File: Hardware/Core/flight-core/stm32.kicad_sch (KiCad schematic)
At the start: 32 parts, among them J7 Conn_01x04_Socket, SW1 SW_Push, SW2 SW_Push, U1 TCAN1042VDRQ1, U2 STM32G473CCTx, U3 MCP23S17_SS, U4 MAX7221xWG, U5 CC56-12SEKWA, Y1 48 MHz

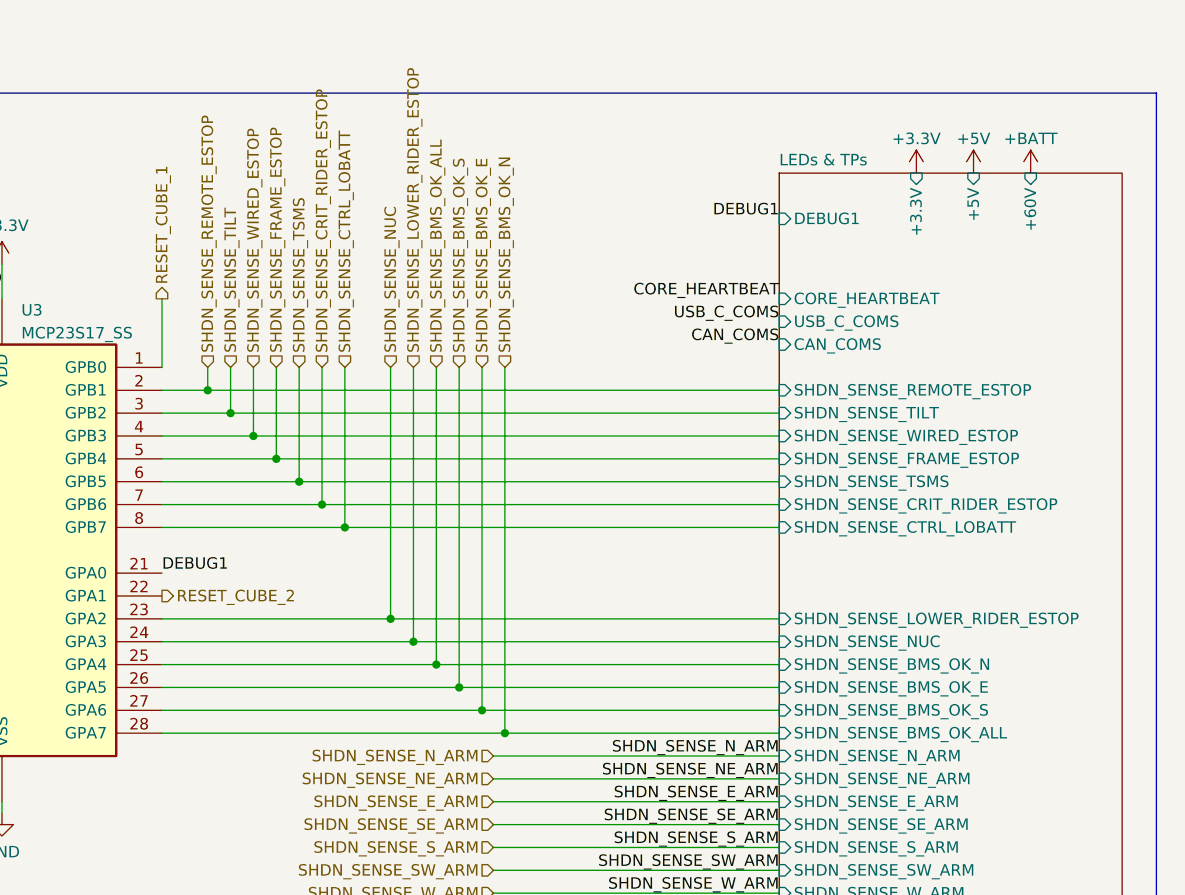
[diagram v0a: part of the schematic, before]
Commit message: adding more stm32 wiring
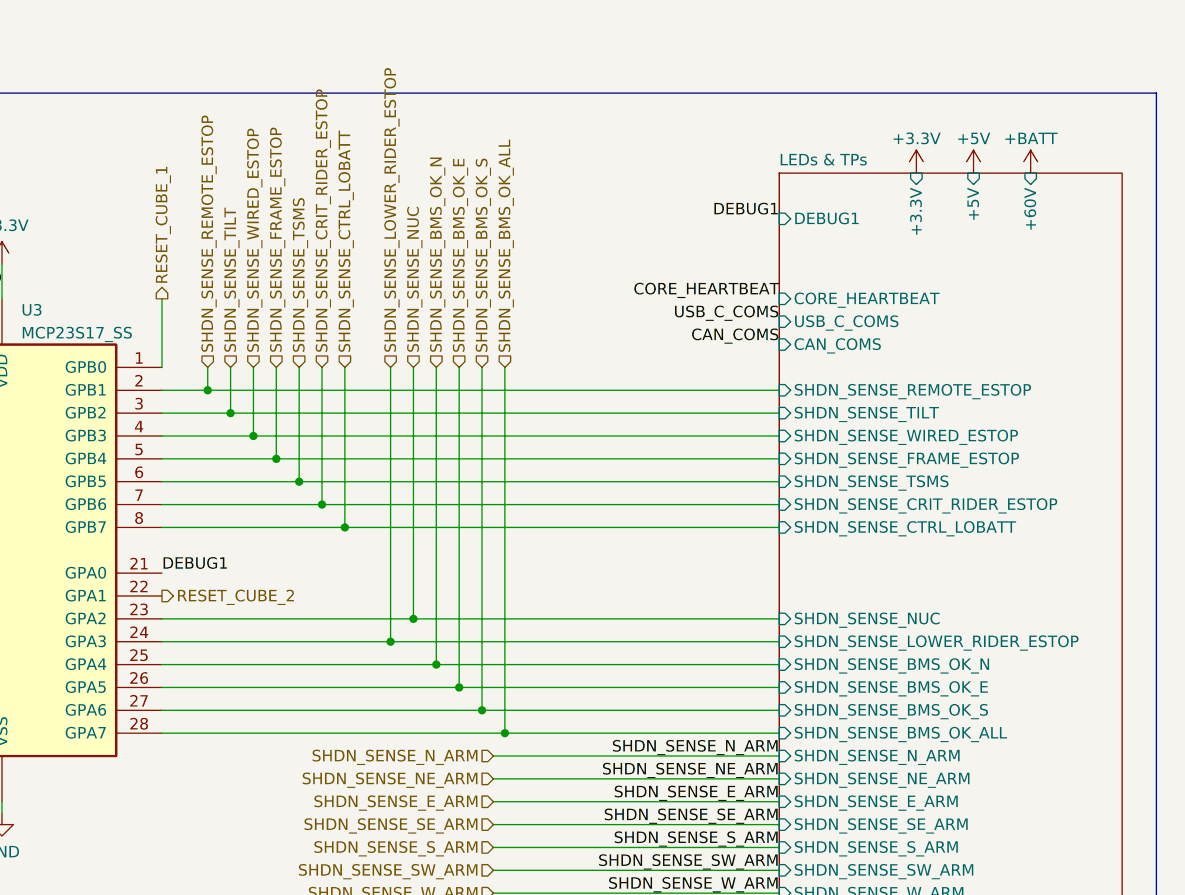
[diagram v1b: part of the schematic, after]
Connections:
- net SHDN_SENSE_BMS_OK_ALL: now also U3.28 (GPA7); no longer U3.25 (GPA4)
- net SHDN_SENSE_BMS_OK_E: now also U3.26 (GPA5); no longer U3.27 (GPA6)
- net SHDN_SENSE_BMS_OK_N: now also U3.25 (GPA4); no longer U3.28 (GPA7)
- net SHDN_SENSE_BMS_OK_S: now also U3.27 (GPA6); no longer U3.26 (GPA5)

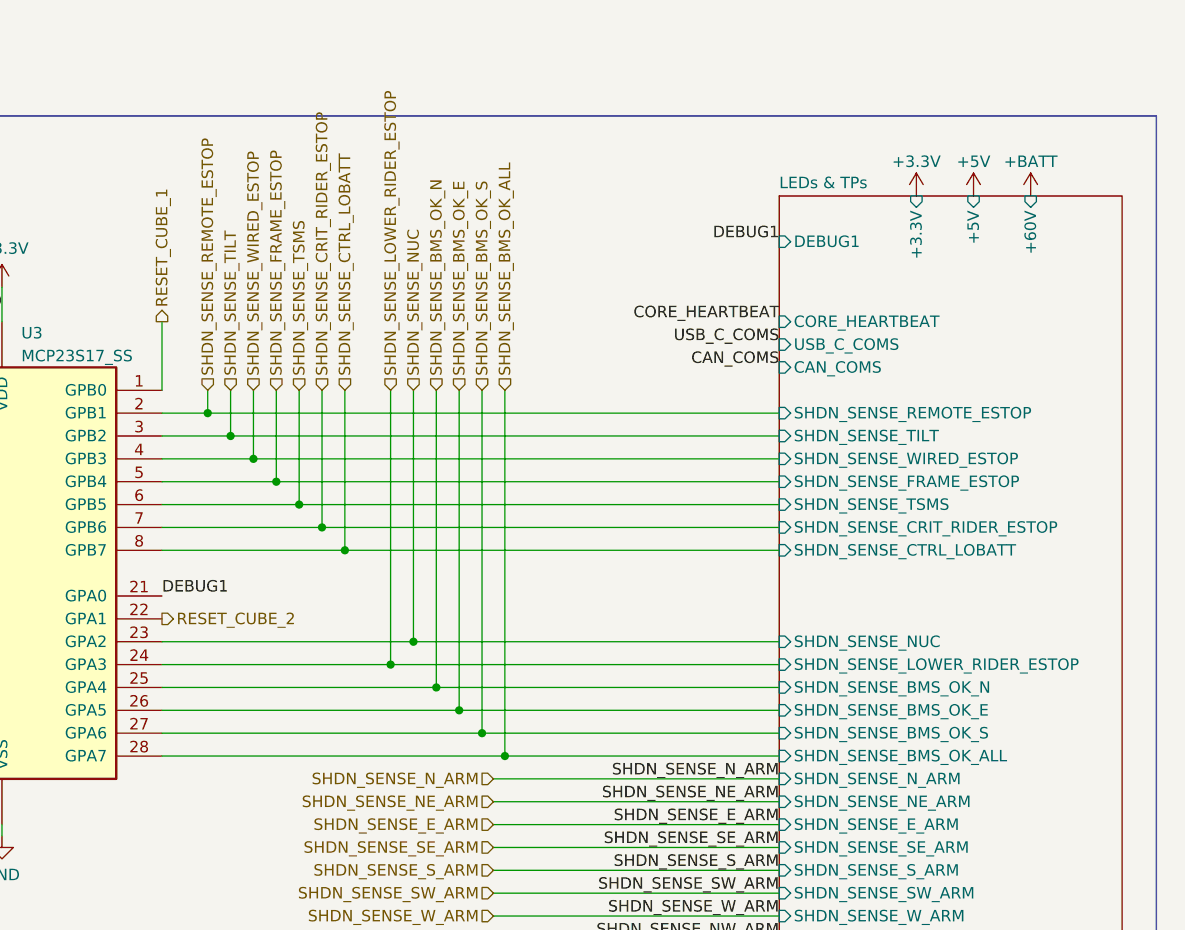
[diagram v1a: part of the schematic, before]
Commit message: routed almost everything except 3.3V power and CAN+/-
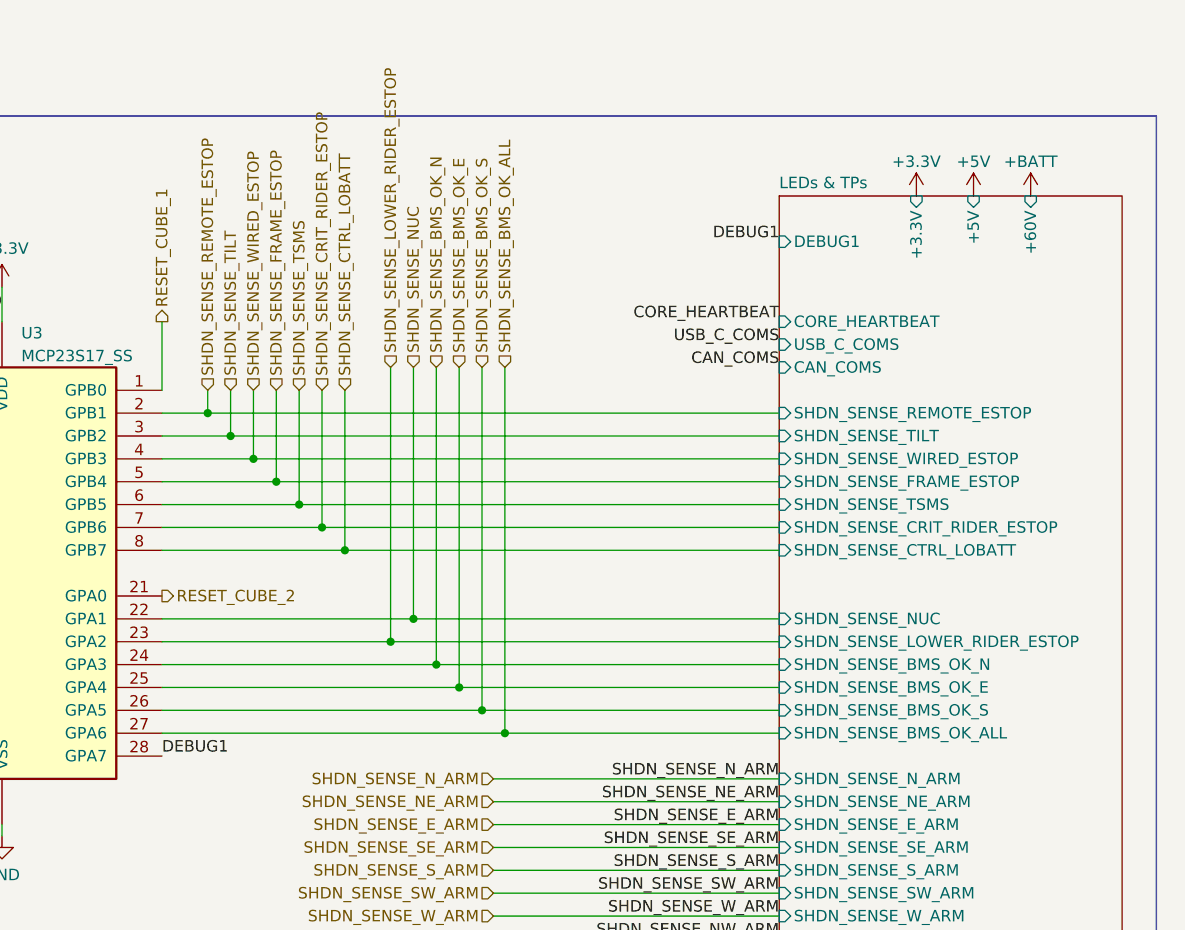
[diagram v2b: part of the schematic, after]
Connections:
- net DEBUG1: now also U3.28 (GPA7); no longer U3.21 (GPA0)
- net RESET_CUBE_2: now also U3.21 (GPA0); no longer U3.22 (GPA1)
- net SHDN_SENSE_BMS_OK_ALL: now also U3.27 (GPA6); no longer U3.28 (GPA7)
- net SHDN_SENSE_BMS_OK_E: now also U3.25 (GPA4); no longer U3.26 (GPA5)
- net SHDN_SENSE_BMS_OK_N: now also U3.24 (GPA3); no longer U3.25 (GPA4)
- net SHDN_SENSE_BMS_OK_S: now also U3.26 (GPA5); no longer U3.27 (GPA6)
- net SHDN_SENSE_LOWER_RIDER_ESTOP: now also U3.23 (GPA2); no longer U3.24 (GPA3)
- net SHDN_SENSE_NUC: now also U3.22 (GPA1); no longer U3.23 (GPA2)
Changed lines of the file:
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@@
 	)
 	(junction
-		(at 198.12 77.47)
+		(at 198.12 74.93)
 		(diameter 0)
 		(color 0 0 0 0)
@@
 	)
 	(junction
-		(at 205.74 87.63)
+		(at 205.74 85.09)
 		(diameter 0)
 		(color 0 0 0 0)
@@
 	)
 	(junction
-		(at 195.58 80.01)
+		(at 195.58 77.47)
 		(diameter 0)
 		(color 0 0 0 0)
@@
 	)
 	(junction
-		(at 200.66 82.55)
+		(at 200.66 80.01)
 		(diameter 0)
 		(color 0 0 0 0)
@@
 	)
 	(junction
-		(at 208.28 90.17)
+		(at 208.28 87.63)
 		(diameter 0)
 		(color 0 0 0 0)
@@
 	)
 	(junction
-		(at 203.2 85.09)
+		(at 203.2 82.55)
 		(diameter 0)
 		(color 0 0 0 0)
@@
 	(wire
 		(pts
-			(xy 170.18 90.17) (xy 208.28 90.17)
+			(xy 170.18 87.63) (xy 208.28 87.63)
 		)
 		(stroke
@@
 	(wire
 		(pts
-			(xy 203.2 49.53) (xy 203.2 85.09)
+			(xy 203.2 46.99) (xy 203.2 82.55)
 		)
 		(stroke
@@
 	(wire
 		(pts
-			(xy 198.12 49.53) (xy 198.12 77.47)
+			(xy 198.12 46.99) (xy 198.12 74.93)
 		)
 		(stroke
@@
 	(wire
 		(pts
-			(xy 170.18 77.47) (xy 198.12 77.47)
+			(xy 170.18 74.93) (xy 198.12 74.93)
 		)
 		(stroke
@@
 	(wire
 		(pts
-			(xy 205.74 49.53) (xy 205.74 87.63)
+			(xy 205.74 46.99) (xy 205.74 85.09)
 		)
 		(stroke
@@
 	(wire
 		(pts
-			(xy 170.18 80.01) (xy 195.58 80.01)
+			(xy 170.18 77.47) (xy 195.58 77.47)
 		)
 		(stroke
@@
 	(wire
 		(pts
-			(xy 195.58 80.01) (xy 238.76 80.01)
+			(xy 195.58 77.47) (xy 238.76 77.47)
 		)
 		(stroke
@@
 	(wire
 		(pts
-			(xy 170.18 87.63) (xy 205.74 87.63)
+			(xy 170.18 85.09) (xy 205.74 85.09)
 		)
 		(stroke
@@
 	(wire
 		(pts
-			(xy 203.2 85.09) (xy 238.76 85.09)
+			(xy 203.2 82.55) (xy 238.76 82.55)
 		)
 		(stroke
@@
 	(wire
 		(pts
-			(xy 205.74 87.63) (xy 238.76 87.63)
+			(xy 205.74 85.09) (xy 238.76 85.09)
 		)
 		(stroke
@@
 	(wire
 		(pts
-			(xy 195.58 49.53) (xy 195.58 80.01)
+			(xy 195.58 46.99) (xy 195.58 77.47)
 		)
 		(stroke
@@
 	(wire
 		(pts
-			(xy 200.66 49.53) (xy 200.66 82.55)
+			(xy 200.66 46.99) (xy 200.66 80.01)
 		)
 		(stroke
@@
 	(wire
 		(pts
-			(xy 208.28 90.17) (xy 238.76 90.17)
+			(xy 208.28 87.63) (xy 238.76 87.63)
 		)
 		(stroke
@@
 	(wire
 		(pts
-			(xy 170.18 82.55) (xy 200.66 82.55)
+			(xy 170.18 80.01) (xy 200.66 80.01)
 		)
 		(stroke
@@
 	(wire
 		(pts
-			(xy 170.18 85.09) (xy 203.2 85.09)
+			(xy 170.18 82.55) (xy 203.2 82.55)
 		)
 		(stroke
@@
 	(wire
 		(pts
-			(xy 208.28 49.53) (xy 208.28 90.17)
+			(xy 208.28 46.99) (xy 208.28 87.63)
 		)
 		(stroke
@@
 	(wire
 		(pts
-			(xy 198.12 77.47) (xy 238.76 77.47)
+			(xy 198.12 74.93) (xy 238.76 74.93)
 		)
 		(stroke
@@
 	(wire
 		(pts
-			(xy 200.66 82.55) (xy 238.76 82.55)
+			(xy 200.66 80.01) (xy 238.76 80.01)
 		)
 		(stroke
@@
 	)
 	(label "DEBUG1"
-		(at 170.18 72.39 0)
+		(at 170.18 90.17 0)
 		(effects
 			(font
@@
 	(hierarchical_label "SHDN_SENSE_LOWER_RIDER_ESTOP"
 		(shape input)
-		(at 195.58 49.53 90)
+		(at 195.58 46.99 90)
 		(effects
 			(font
@@
 	(hierarchical_label "SHDN_SENSE_BMS_OK_N"
 		(shape input)
-		(at 200.66 49.53 90)
+		(at 200.66 46.99 90)
 		(effects
 			(font
@@
 	(hierarchical_label "SHDN_SENSE_NUC"
 		(shape input)
-		(at 198.12 49.53 90)
+		(at 198.12 46.99 90)
 		(effects
 			(font
@@
 	(hierarchical_label "SHDN_SENSE_BMS_OK_S"
 		(shape input)
-		(at 205.74 49.53 90)
+		(at 205.74 46.99 90)
 		(effects
 			(font
@@
 	(hierarchical_label "SHDN_SENSE_BMS_OK_E"
 		(shape input)
-		(at 203.2 49.53 90)
+		(at 203.2 46.99 90)
 		(effects
 			(font
@@
 	(hierarchical_label "RESET_CUBE_2"
 		(shape output)
-		(at 170.18 74.93 0)
+		(at 170.18 72.39 0)
 		(effects
 			(font
@@
 	(hierarchical_label "SHDN_SENSE_BMS_OK_ALL"
 		(shape input)
-		(at 208.28 49.53 90)
+		(at 208.28 46.99 90)
 		(effects
 			(font
@@
 		)
 		(pin "SHDN_SENSE_BMS_OK_ALL" input
-			(at 238.76 90.17 180)
+			(at 238.76 87.63 180)
 			(effects
 				(font
@@
 		)
 		(pin "SHDN_SENSE_BMS_OK_S" input
-			(at 238.76 87.63 180)
+			(at 238.76 85.09 180)
 			(effects
 				(font
@@
 		)
 		(pin "SHDN_SENSE_BMS_OK_E" input
-			(at 238.76 85.09 180)
+			(at 238.76 82.55 180)
 			(effects
 				(font
@@
 		)
 		(pin "SHDN_SENSE_BMS_OK_N" input
-			(at 238.76 82.55 180)
+			(at 238.76 80.01 180)
 			(effects
 				(font
@@
 		)
 		(pin "SHDN_SENSE_NUC" input
-			(at 238.76 77.47 180)
+			(at 238.76 74.93 180)
 			(effects
 				(font
@@
 		)
 		(pin "SHDN_SENSE_LOWER_RIDER_ESTOP" input
-			(at 238.76 80.01 180)
+			(at 238.76 77.47 180)
 			(effects
 				(font

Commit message: Major reroute & semi-final update
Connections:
- net CAN_COMS: now also U2.43 (PB6); no longer U2.44 (PB7)
- net DEBUG1: now also U3.21 (GPA0); no longer U3.28 (GPA7)
- net RESET_CUBE_2: now also U3.22 (GPA1); no longer U3.21 (GPA0)
- net SHDN_SENSE_BMS_OK_ALL: now also U3.28 (GPA7); no longer U3.27 (GPA6)
- net SHDN_SENSE_BMS_OK_E: now also U3.26 (GPA5); no longer U3.25 (GPA4)
- net SHDN_SENSE_BMS_OK_N: now also U3.25 (GPA4); no longer U3.24 (GPA3)
- net SHDN_SENSE_BMS_OK_S: now also U3.27 (GPA6); no longer U3.26 (GPA5)
- net SHDN_SENSE_LOWER_RIDER_ESTOP: now also U3.24 (GPA3); no longer U3.23 (GPA2)
- net SHDN_SENSE_NUC: now also U3.23 (GPA2); no longer U3.22 (GPA1)
- net USB_C_COMS: now also U2.44 (PB7); no longer U2.43 (PB6)
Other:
- sheet LEDs & TPs ports: added none; removed +60V

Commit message: minor reformatting; no substantial changes
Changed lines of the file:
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@@
 	(wire
 		(pts
-			(xy 203.2 46.99) (xy 203.2 85.09)
+			(xy 203.2 49.53) (xy 203.2 85.09)
 		)
 		(stroke
@@
 	(wire
 		(pts
-			(xy 205.74 46.99) (xy 205.74 87.63)
+			(xy 205.74 49.53) (xy 205.74 87.63)
 		)
 		(stroke
@@
 	(wire
 		(pts
-			(xy 198.12 46.99) (xy 198.12 77.47)
+			(xy 198.12 49.53) (xy 198.12 77.47)
 		)
 		(stroke
@@
 	(wire
 		(pts
-			(xy 208.28 46.99) (xy 208.28 90.17)
+			(xy 208.28 49.53) (xy 208.28 90.17)
 		)
 		(stroke
@@
 	(wire
 		(pts
-			(xy 200.66 46.99) (xy 200.66 82.55)
+			(xy 200.66 49.53) (xy 200.66 82.55)
 		)
 		(stroke
@@
 	(wire
 		(pts
-			(xy 195.58 46.99) (xy 195.58 80.01)
+			(xy 195.58 49.53) (xy 195.58 80.01)
 		)
 		(stroke
@@
 	(hierarchical_label "SHDN_SENSE_LOWER_RIDER_ESTOP"
 		(shape input)
-		(at 195.58 46.99 90)
+		(at 195.58 49.53 90)
 		(effects
 			(font
@@
 	(hierarchical_label "SHDN_SENSE_BMS_OK_N"
 		(shape input)
-		(at 200.66 46.99 90)
+		(at 200.66 49.53 90)
 		(effects
 			(font
@@
 	(hierarchical_label "SHDN_SENSE_NUC"
 		(shape input)
-		(at 198.12 46.99 90)
+		(at 198.12 49.53 90)
 		(effects
 			(font
@@
 	(hierarchical_label "SHDN_SENSE_BMS_OK_S"
 		(shape input)
-		(at 205.74 46.99 90)
+		(at 205.74 49.53 90)
 		(effects
 			(font
@@
 	(hierarchical_label "SHDN_SENSE_BMS_OK_E"
 		(shape input)
-		(at 203.2 46.99 90)
+		(at 203.2 49.53 90)
 		(effects
 			(font
@@
 	(hierarchical_label "SHDN_SENSE_BMS_OK_ALL"
 		(shape input)
-		(at 208.28 46.99 90)
-		(effects
-			(font
+		(at 208.28 49.53 90)
+		(effects
+			(font
